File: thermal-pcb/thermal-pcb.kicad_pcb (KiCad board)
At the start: 2 copper layers, 98 x 56 mm, 63 parts, among them J1 FALLBACK_IN, J2 Conn_01x14_Pin, J3 USB_C_Receptacle_USB2.0_16P, J4 Conn_01x04_Socket, J5 BATT_CONN, Q1 FS8205A, Q2 AO3415, U1 ESP32-S3-WROOM-1, U2 MCP73871, U3 MIC5504-3.3YM5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

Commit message: add firmware
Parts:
- added H1: MountingHole, MountingHole:MountingHole_4.3mm_M4, F.Cu at (166.5, 90.0)
- added H2: MountingHole, MountingHole:MountingHole_4.3mm_M4, F.Cu at (138.8, 104.2)
- added H3: MountingHole, MountingHole:MountingHole_4.3mm_M4, F.Cu at (111.5, 96.0)
- added H4: MountingHole, MountingHole:MountingHole_4.3mm_M4, F.Cu at (175.0, 127.8)
- added SW1: MFS201N-16-Z, Component:MFS201N-16-Z_NDC, F.Cu at (141.5, 131.7)
- Q1: value FS8205A -> FS8205; footprint Component:SOP65P640X120-8N -> Component:SOT95P280X145-6N
- moved Q2 7.86 mm to (136.8, 122.8), turned to 180 degrees
- moved R4 2.20 mm to (156.2, 114.5), turned to 0 degrees
- moved TP9 1.87 mm to (156.0, 111.5)
- moved Q1 1.86 mm to (157.8, 108.5), turned to 180 degrees
- turned C1 to -90 degrees
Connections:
- Q1 pad 1: Net-(Q1-Pad1) -> -BATT
- Q1 pad 2: -BATT -> Net-(Q1-Pad2)
- Q1 pad 4: Net-(U4-OD) -> Net-(U4-OC)
- Q1 pad 5: Net-(U4-OC) -> Net-(Q1-Pad2)
- Q1 pad 6: -BATT -> Net-(U4-OD)
- Q2 pad 3: Net-(J5-Pin_1) -> Net-(Q2-D)
- TP9 pad 1: Net-(Q1-Pad1) -> Net-(Q1-Pad2)
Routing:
- net Net-(Q2-D): track 0.00 -> 14.4 mm
- net +BATT: track 61.8 -> 48.3 mm, vias 7 -> 5
- net Net-(J5-Pin_1): track 9.11 -> 19.0 mm
- net Net-(Q1-Pad1): track 9.38 -> 0.00 mm
- net -BATT: track 52.8 -> 43.8 mm, vias 59 -> 58
- net Net-(U4-VCC): track 10.5 -> 17.0 mm
- net Net-(Q1-Pad2): track 0.00 -> 6.28 mm
- net Net-(U4-OD): track 4.94 -> 7.54 mm
- net Net-(U4-OC): track 10.4 -> 11.8 mm, vias 0 -> 2

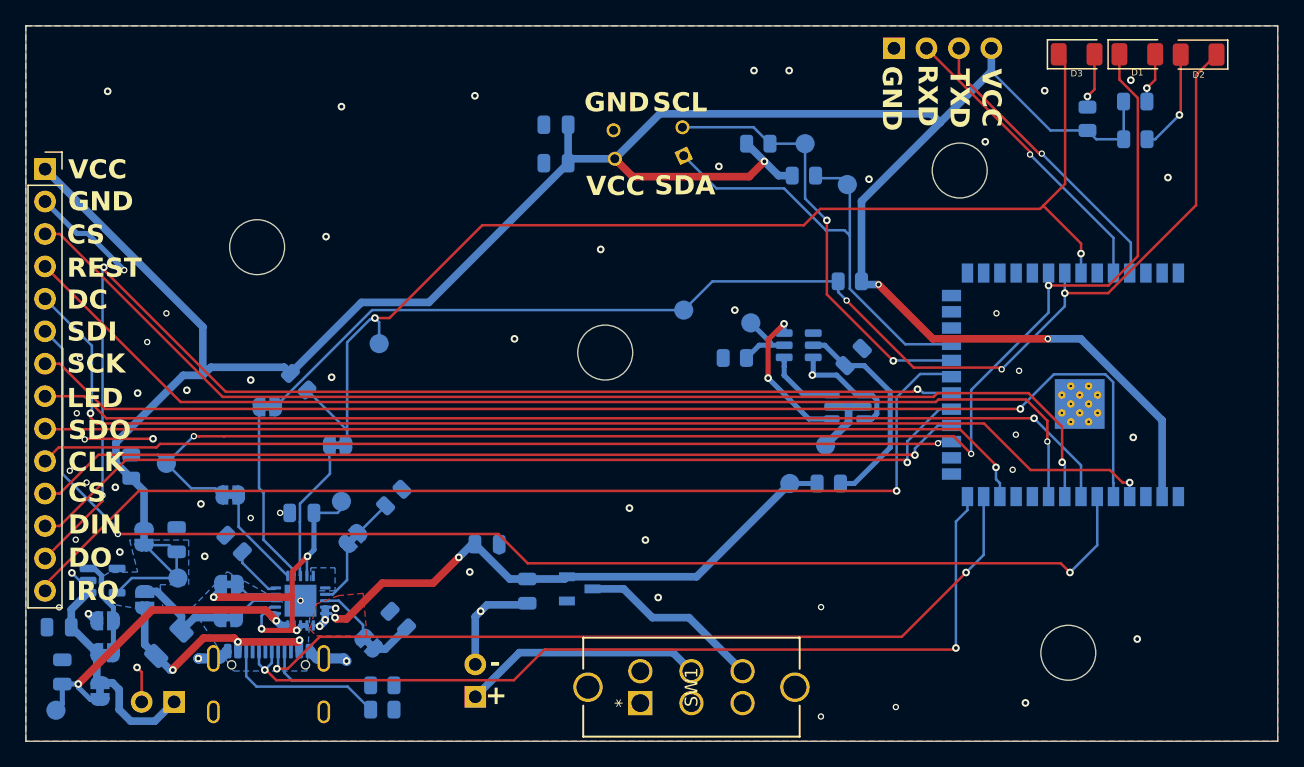
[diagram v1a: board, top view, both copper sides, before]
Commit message: update pcb + bom to use aliexpress stuff
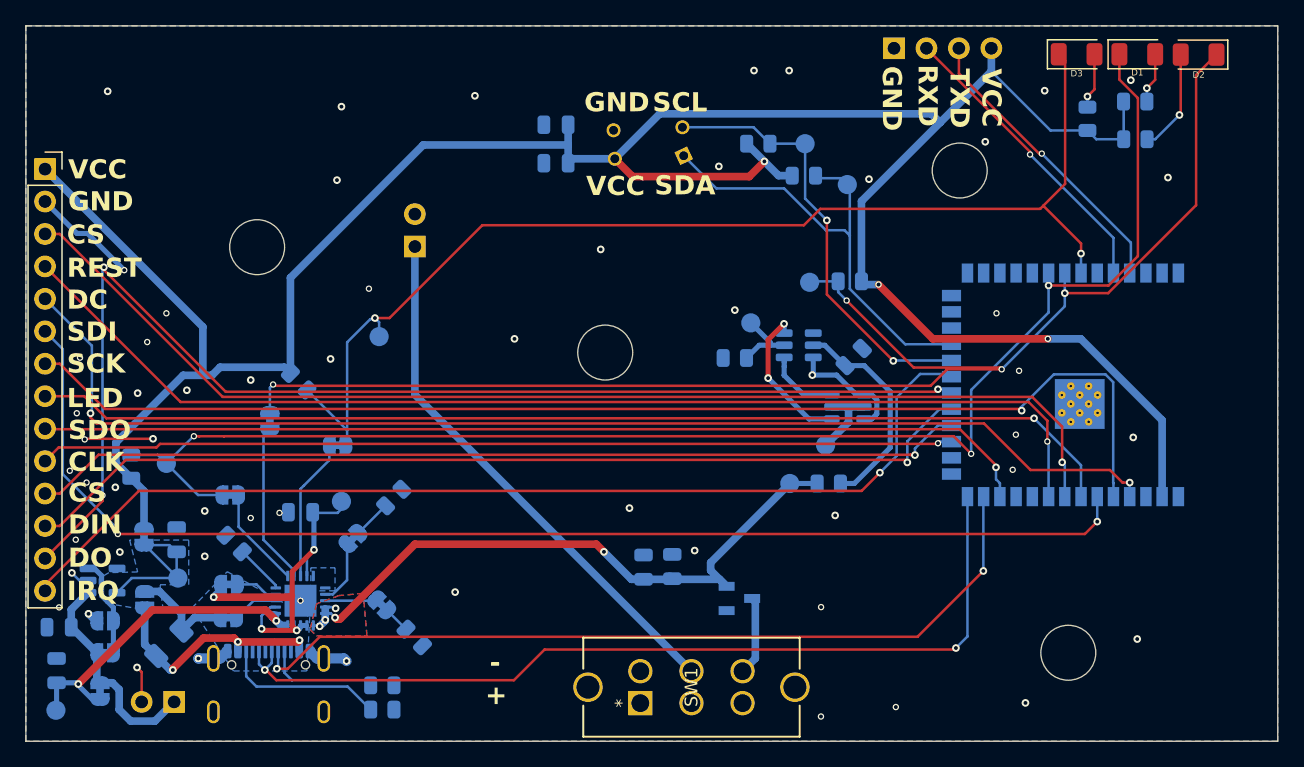
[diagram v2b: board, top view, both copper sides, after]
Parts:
- moved J5 35.6 mm to (123.8, 96.0)
- moved Q2 12.5 mm to (149.2, 123.5)
- moved C7 12.4 mm to (141.8, 121.1), turned to 90 degrees
- moved C1 11.5 mm to (144.0, 121.0), turned to 90 degrees
- moved TP6 10.1 mm to (154.8, 98.8)
- moved JP3 3.16 mm to (121.2, 124.0)
- moved R10 1.87 mm to (123.8, 126.5), turned to 135 degrees
- moved JP9 1.12 mm to (112.5, 109.6), turned to 90 degrees
- moved TP7 0.55 mm to (121.0, 103.0)
- moved C2 0.46 mm to (95.8, 129.2)
- moved C3 0.11 mm to (114.9, 116.8)
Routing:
- net Net-(J5-Pin_1): track 19.0 -> 42.2 mm
- net STAT2: track 99.4 -> 113.5 mm, vias 3 -> 4
- net -BATT: track 43.8 -> 35.0 mm
- net Net-(Q2-D): track 14.4 -> 6.21 mm
- net VCC: track 197.2 -> 202.1 mm
- net +BATT: track 48.3 -> 51.9 mm
- net LCD_SDI: track 100.8 -> 97.3 mm
- net Net-(JP9-A): track 14.4 -> 12.7 mm
- net LCD_T_IRQ: track 82.7 -> 81.0 mm
- net Net-(JP3-A): track 3.18 -> 2.04 mm
- net VBUS: track 37.1 -> 38.2 mm
- net USB_D-: track 67.6 -> 68.4 mm
- net Net-(JP3-B): track 4.71 -> 4.01 mm
- net STAT1: track 92.9 -> 92.3 mm
- added copper zone on B.Cu, net +BATT
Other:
- board text added: "(6/10/2025)"
